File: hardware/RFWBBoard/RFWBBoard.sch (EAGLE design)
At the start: 87 parts, among them IC1 24LC025ST, J1 CON-71742-2184-BOT, M1 MOUNT-HOLE3.3, M2 MOUNT-HOLE3.3, M3 MOUNT-HOLE3.3, M4 MOUNT-HOLE3.3, U1 MAX2830IPC-7351, U2 LDB212G4010C-001, U3 LDB212G4010C-001, U4 AD8132MSOP8, U5 AD8132MSOP8, U6 AD8132MSOP8, U7 AD8132MSOP8, X1 LTI-SASF54GT, X2 LTI-SASF54GT, X4 LTI-SASF54GT, X5 LTI-SASF54GT, X6 LTI-SASF54GT, X7 LTI-SASF54GT

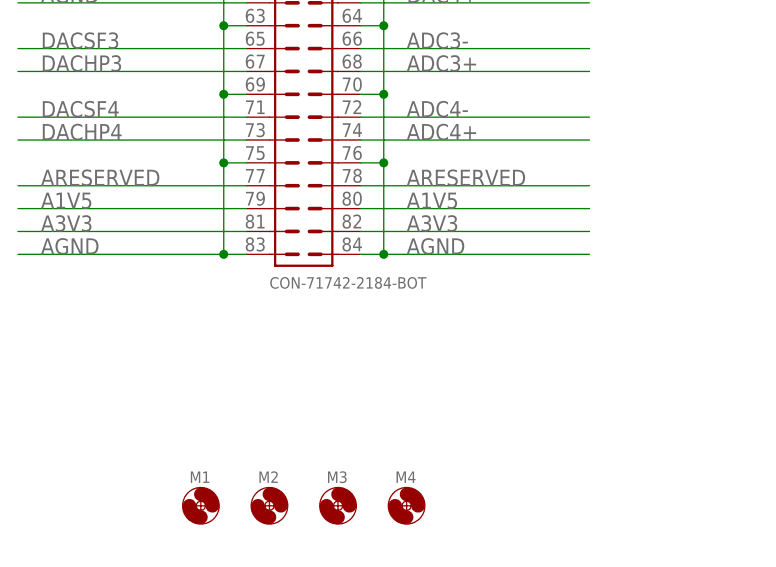
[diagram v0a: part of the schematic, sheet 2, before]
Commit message: - Schematic updated - Info text updated on PCB back - 84 pin component changed in library
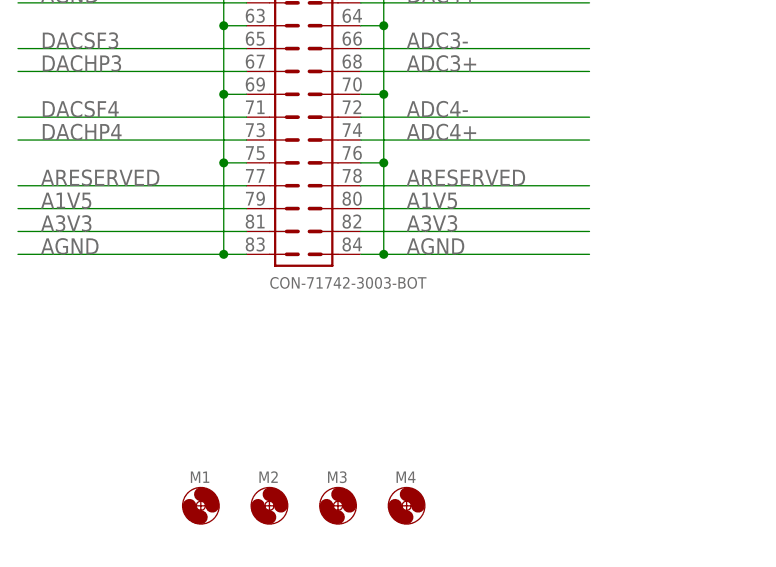
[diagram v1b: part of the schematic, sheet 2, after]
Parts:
- J1: value CON-71742-2184-BOT -> CON-71742-3003-BOT; device RFWBBoard:CON-71742-2184-BOT -> RFWBBoard:CON-71742-3003-BOT
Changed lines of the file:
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@@
 <attribute name="PAGE4" value="Control/Digital Signals"/>
 <attribute name="PAGE5" value="Supply"/>
+<attribute name="REVIEWER1" value="Peter Volgyesi"/>
+<attribute name="REVIEWER2" value="Sandor Szilvasi"/>
+<attribute name="REVIEWEREMAIL1" value="peter.volgyesi@vanderbilt.edu"/>
+<attribute name="REVIEWEREMAIL2" value="sandor.szilvasi@vanderbilt.edu"/>
 <attribute name="REVISION" value="A"/>
 <attribute name="TITLE" value="Radio Front-End Board"/>
-<attribute name="VERIFIER1" value="Peter Volgyesi"/>
-<attribute name="VERIFIER2" value="Sandor Szilvasi"/>
-<attribute name="VERIFIEREMAIL1" value="peter.volgyesi@vanderbilt.edu"/>
-<attribute name="VERIFIEREMAIL2" value="sandor.szilvasi@vanderbilt.edu"/>
 </attributes>
 <variantdefs>
@@
 <part name="M3" library="RFWBBoard" deviceset="MOUNT-HOLE" device="3.3"/>
 <part name="M4" library="RFWBBoard" deviceset="MOUNT-HOLE" device="3.3"/>
-<part name="J1" library="RFWBBoard" deviceset="CON-71742" device="84-BOT" technology="-21"/>
+<part name="J1" library="RFWBBoard" deviceset="CON-71742" device="-3003-BOT"/>
 <part name="FRAME3" library="RFWBBoard" deviceset="FRAME-LETTER" device=""/>
 <part name="U1" library="RFWBBoard" deviceset="MAX2830" device="IPC-7351"/>
@@
 <text x="163.83" y="20.32" size="2.54" layer="95" rot="MR0">&gt;AUTHOREMAIL</text>
 <text x="82.55" y="20.32" size="2.54" layer="95">&gt;AUTHOR</text>
-<text x="82.55" y="7.62" size="2.54" layer="95">&gt;VERIFIER1</text>
-<text x="163.83" y="7.62" size="2.54" layer="95" rot="MR0">&gt;VERIFIEREMAIL1</text>
+<text x="82.55" y="7.62" size="2.54" layer="95">&gt;REVIEWER1</text>
+<text x="163.83" y="7.62" size="2.54" layer="95" rot="MR0">&gt;REVIEWEREMAIL1</text>
 <text x="83.82" y="93.98" size="5.08" layer="97">for the Marmote platform</text>
-<text x="82.55" y="2.54" size="2.54" layer="95">&gt;VERIFIER2</text>
-<text x="163.83" y="2.54" size="2.54" layer="95" rot="MR0">&gt;VERIFIEREMAIL2</text>
+<text x="82.55" y="2.54" size="2.54" layer="95">&gt;REVIEWER2</text>
+<text x="163.83" y="2.54" size="2.54" layer="95" rot="MR0">&gt;REVIEWEREMAIL2</text>
 </plain>
 <instances>

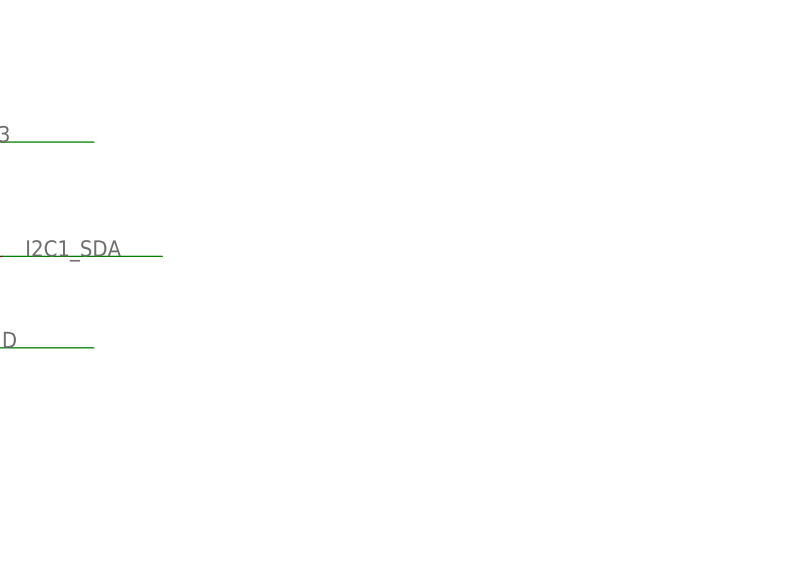
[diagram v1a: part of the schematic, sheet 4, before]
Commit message: - Pull-up resistors for I2C lines
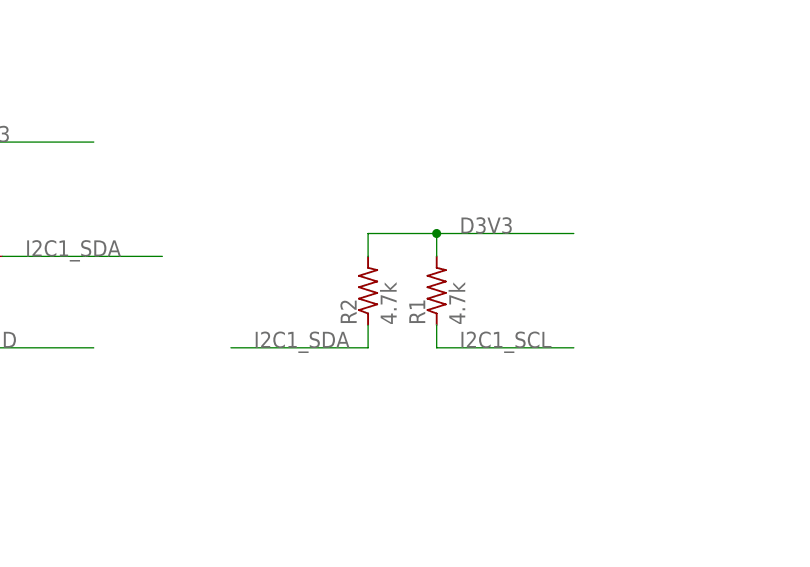
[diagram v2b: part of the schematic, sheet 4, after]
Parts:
- added R1, R2: 4.7k, RFWBBoard:R0402
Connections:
- net D3V3: now also R1.2, R2.2
- net I2C1_SCL: now also R1.1
- net I2C1_SDA: now also R2.1
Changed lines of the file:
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@@
 <?xml version="1.0" encoding="utf-8"?>
 <!DOCTYPE eagle SYSTEM "eagle.dtd">
-<eagle version="6.0">
+<eagle version="6.1">
 <drawing>
 <settings>
@@
 <part name="LOGO2" library="Logo" deviceset="LOGO-MARMOTE-600MIL" device="-10MM-AU"/>
 <part name="LOGO3" library="Logo" deviceset="LOGO-VANDERBILT-600MIL" device="-10MM-AU"/>
+<part name="R1" library="RFWBBoard" deviceset="R" device="0402" value="4.7k"/>
+<part name="R2" library="RFWBBoard" deviceset="R" device="0402" value="4.7k"/>
 </parts>
 <sheets>
@@
 <instance part="RA00" gate="G$1" x="106.68" y="25.4"/>
 <instance part="RA01" gate="G$1" x="106.68" y="15.24"/>
+<instance part="R1" gate="G$1" x="220.98" y="76.2" rot="R90"/>
+<instance part="R2" gate="G$1" x="213.36" y="76.2" rot="R90"/>
 </instances>
 <busses>
@@
 <wire x1="91.44" y1="15.24" x2="101.6" y2="15.24" width="0.1524" layer="91"/>
 </segment>
+<segment>
+<wire x1="236.22" y1="81.28" x2="220.98" y2="81.28" width="0.1524" layer="91"/>
+<pinref part="R2" gate="G$1" pin="2"/>
+<wire x1="220.98" y1="81.28" x2="213.36" y2="81.28" width="0.1524" layer="91"/>
+<wire x1="213.36" y1="81.28" x2="213.36" y2="78.74" width="0.1524" layer="91"/>
+<pinref part="R1" gate="G$1" pin="2"/>
+<wire x1="220.98" y1="78.74" x2="220.98" y2="81.28" width="0.1524" layer="91"/>
+<junction x="220.98" y="81.28"/>
+<label x="223.52" y="81.28" size="1.778" layer="95"/>
+</segment>
 </net>
 <net name="DGND" class="0">
@@
 <label x="175.26" y="78.74" size="1.778" layer="95"/>
 </segment>
+<segment>
+<wire x1="198.12" y1="68.58" x2="213.36" y2="68.58" width="0.1524" layer="91"/>
+<wire x1="213.36" y1="68.58" x2="213.36" y2="71.12" width="0.1524" layer="91"/>
+<label x="200.66" y="68.58" size="1.778" layer="95"/>
+<pinref part="R2" gate="G$1" pin="1"/>
+</segment>
 </net>
 <net name="I2C1_SCL" class="0">
@@
 <label x="129.54" y="86.36" size="1.778" layer="95"/>
 </segment>
-</net>
+<segment>
+<wire x1="220.98" y1="71.12" x2="220.98" y2="68.58" width="0.1524" layer="91"/>
+<wire x1="220.98" y1="68.58" x2="236.22" y2="68.58" width="0.1524" layer="91"/>
+<pinref part="R1" gate="G$1" pin="1"/>
+<label x="223.52" y="68.58" size="1.778" layer="95"/>
+</segment>
+</net>

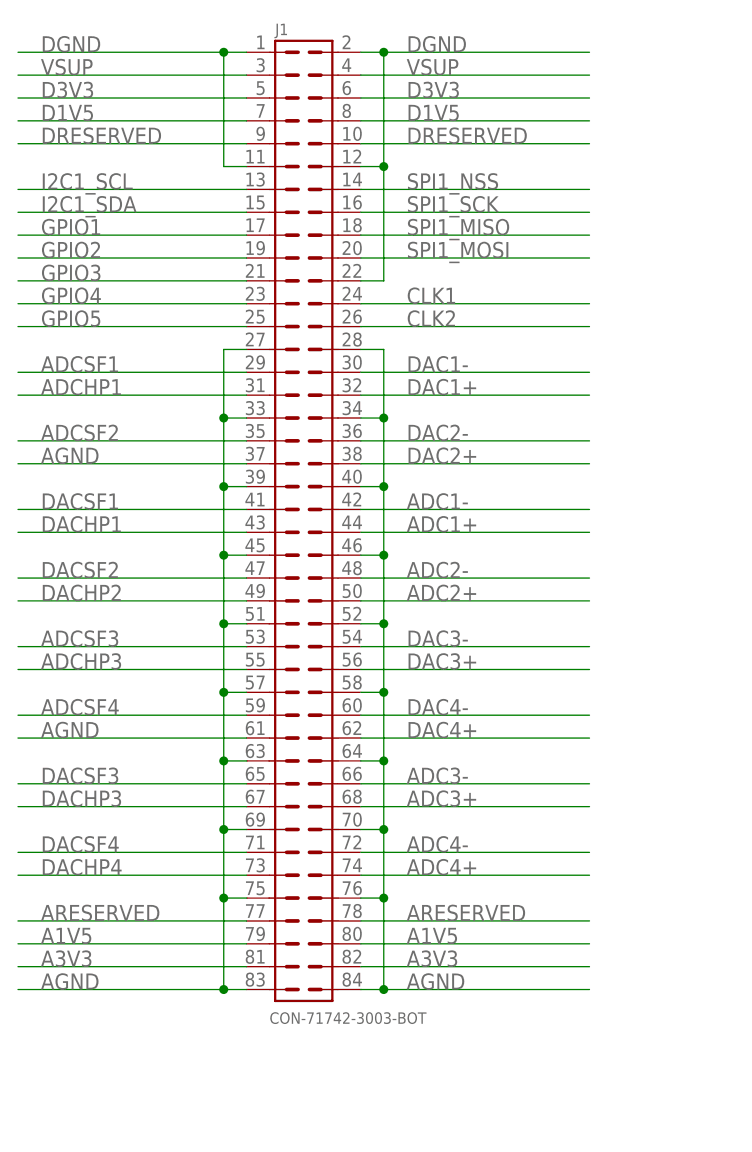
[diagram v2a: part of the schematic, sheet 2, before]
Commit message: - R and C footprints updated from Main Board project - 2.4 GHz and base-band ground part separated with gap - Board layers 4 -> 6 - Interface connector updated
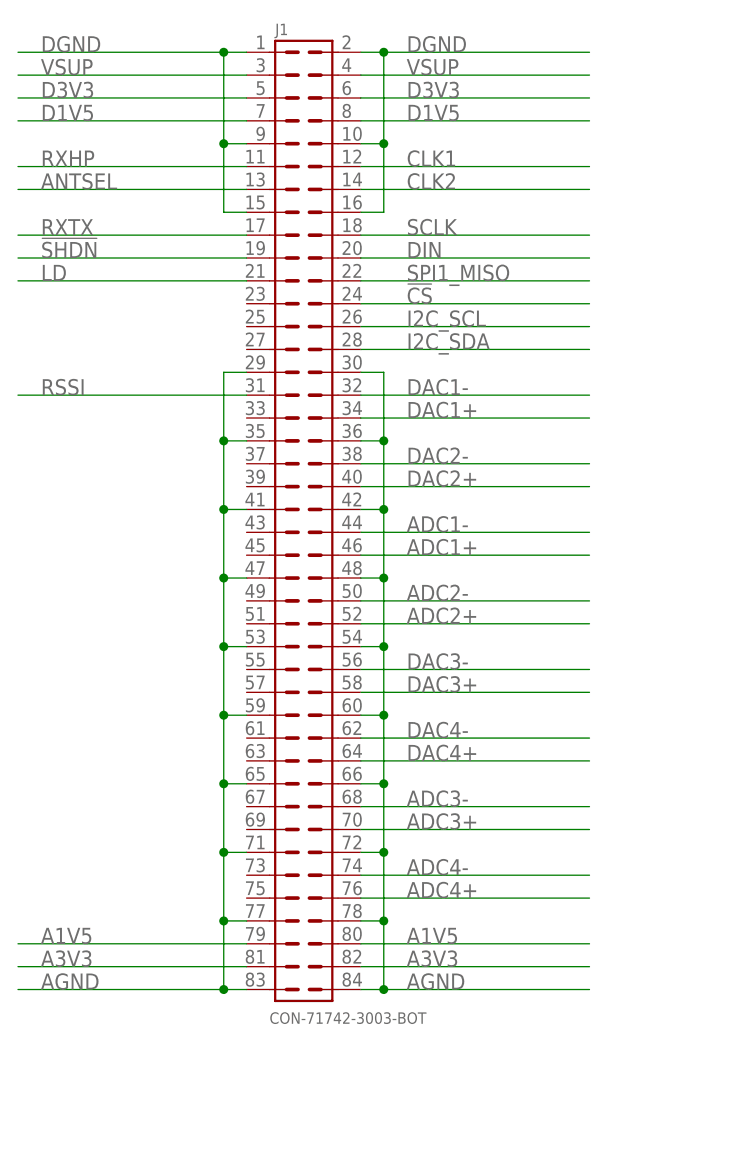
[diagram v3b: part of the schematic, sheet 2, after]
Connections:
- net SPI1_MOSI renamed DIN
- removed net ADCHP1: J1.31
- removed net ADCHP3: J1.55
- removed net ADCSF1: J1.29, U1-CONTROL.RSSI
- removed net ADCSF2: J1.35
- removed net ADCSF3: J1.53
- removed net ADCSF4: J1.59
- removed net ARESERVED: J1.77, J1.78
- removed net DACHP1: J1.43
- removed net DACHP2: J1.49
- removed net DACHP3: J1.67
- removed net DACHP4: J1.73
- removed net DACSF1: J1.41
- removed net DACSF2: J1.47
- removed net DACSF3: J1.65
- removed net DACSF4: J1.71
- removed net DRESERVED: J1.10, J1.9
- removed net GPIO1: J1.17, U1-CONTROL.RXHP
- removed net GPIO2: J1.19, U1-CONTROL.ANTSEL
- removed net GPIO3: J1.21, U1-CONTROL.RXTX
- removed net GPIO4: J1.23, U1-CONTROL./SHDN
- removed net GPIO5: J1.25, U1-PLL-XTAL.LD
- removed net I2C1_SCL: IC1.SCL, J1.13, R1.1
- removed net I2C1_SDA: IC1.SDA, J1.15, R2.1
- removed net SPI1_NSS: J1.14, U1-SERIAL./CS
- removed net SPI1_SCK: J1.16, U1-SERIAL.SCLK
- new net !CS: J1.24, U1-SERIAL./CS
- new net !SHDN: J1.19, U1-CONTROL./SHDN
- new net ANTSEL: J1.13, U1-CONTROL.ANTSEL
- new net I2C_SCL: IC1.SCL, J1.26, R1.1
- new net I2C_SDA: IC1.SDA, J1.28, R2.1
- new net LD: J1.21, U1-PLL-XTAL.LD
- new net RSSI: J1.31, U1-CONTROL.RSSI
- new net RXHP: J1.11, U1-CONTROL.RXHP
- new net RXTX: J1.17, U1-CONTROL.RXTX
- new net SCLK: J1.18, U1-SERIAL.SCLK
- net ADC1+: now also J1.46; no longer J1.44
- net ADC1-: now also J1.44; no longer J1.42
- net ADC2+: now also J1.52; no longer J1.50
- net ADC2-: now also J1.50; no longer J1.48
- net ADC3+: now also J1.70; no longer J1.68
- net ADC3-: now also J1.68; no longer J1.66
- net ADC4+: now also J1.76; no longer J1.74
- net ADC4-: now also J1.74; no longer J1.72
- net AGND: now also J1.29, J1.30, J1.35, J1.36, J1.41, J1.42, J1.47, J1.48, J1.53, J1.54, J1.59, J1.60, J1.65, J1.66, J1.71, J1.72, J1.77, J1.78; no longer J1.27, J1.28, J1.33, J1.34, J1.37, J1.39, J1.40, J1.45, J1.46, J1.51, J1.52, J1.57, J1.58, J1.61, J1.63, J1.64, J1.69, J1.70, J1.75, J1.76
- net CLK1: now also J1.12; no longer J1.24
- net CLK2: now also J1.14; no longer J1.26
- net DAC1+: now also J1.34; no longer J1.32
- net DAC1-: now also J1.32; no longer J1.30
- net DAC2+: now also J1.40; no longer J1.38
- net DAC2-: now also J1.38; no longer J1.36
- net DAC3+: now also J1.58; no longer J1.56
- net DAC3-: now also J1.56; no longer J1.54
- net DAC4+: now also J1.64; no longer J1.62
- net DAC4-: now also J1.62; no longer J1.60
- net DGND: now also J1.10, J1.15, J1.16, J1.9; no longer J1.11, J1.12, J1.22
- net SPI1_MISO: now also J1.22; no longer J1.18
